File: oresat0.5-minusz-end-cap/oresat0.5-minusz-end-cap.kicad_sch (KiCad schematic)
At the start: 35 parts, among them J1 M55-7011242R, J2 U.FL-R-SMA, U1 LTC4305, U2 MMC5983MA, U3 MMC5983MA

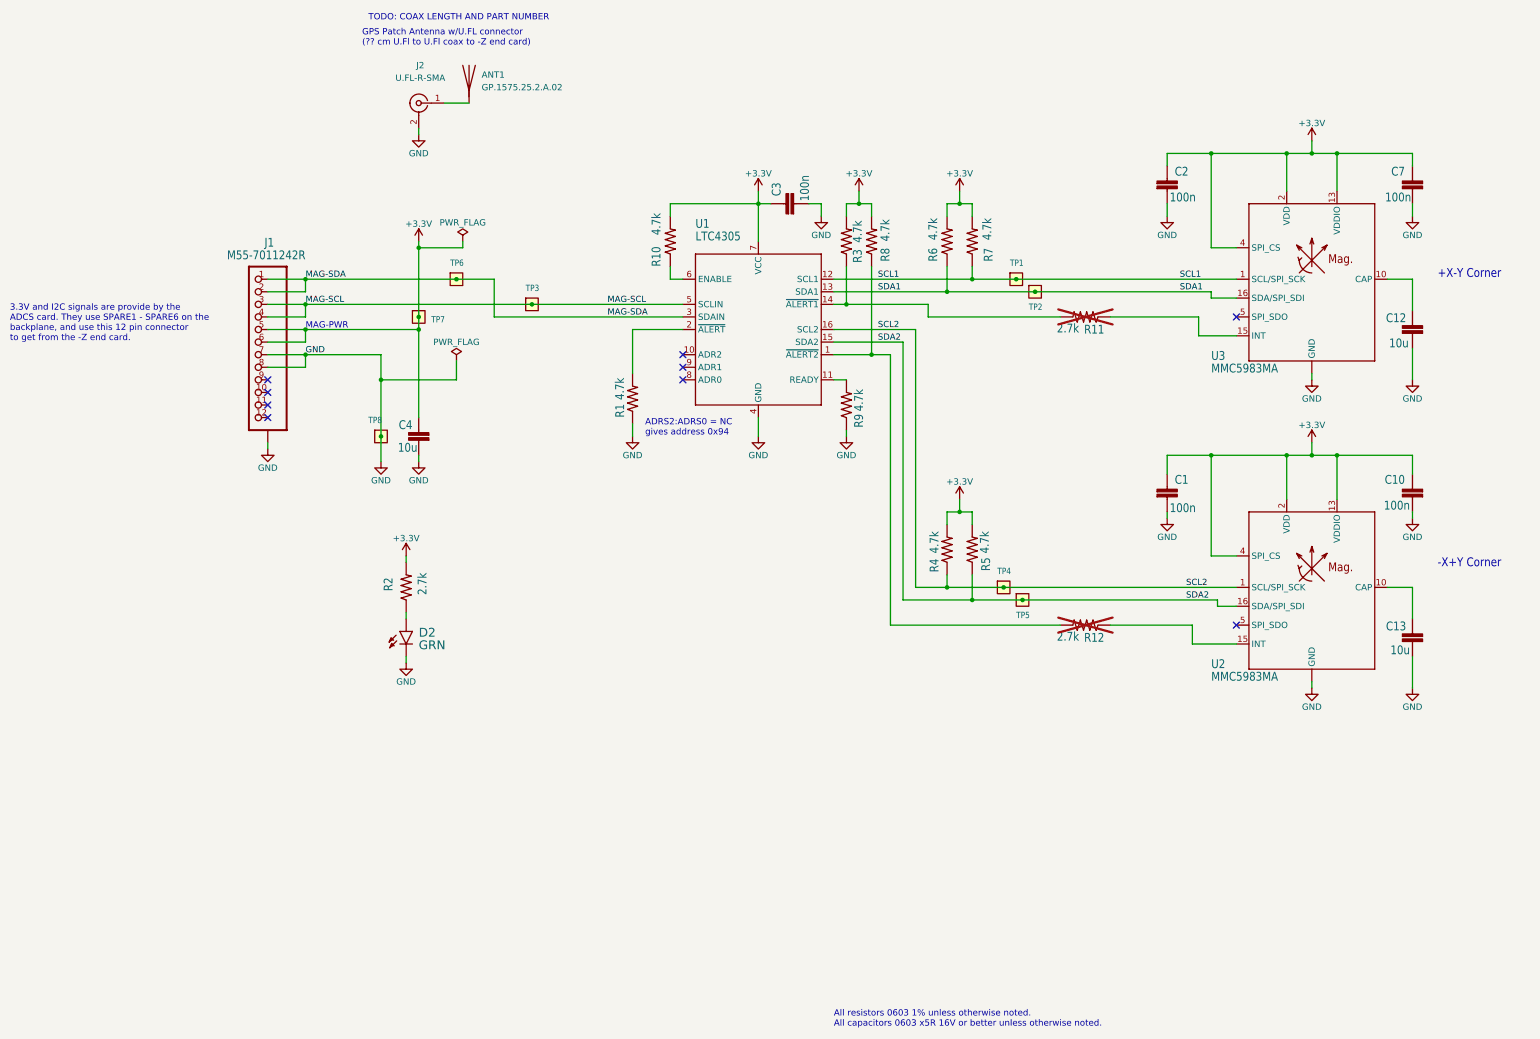
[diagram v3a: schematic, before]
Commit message: Added note on which MAG was which for firmware (PZ1 - MZ2).
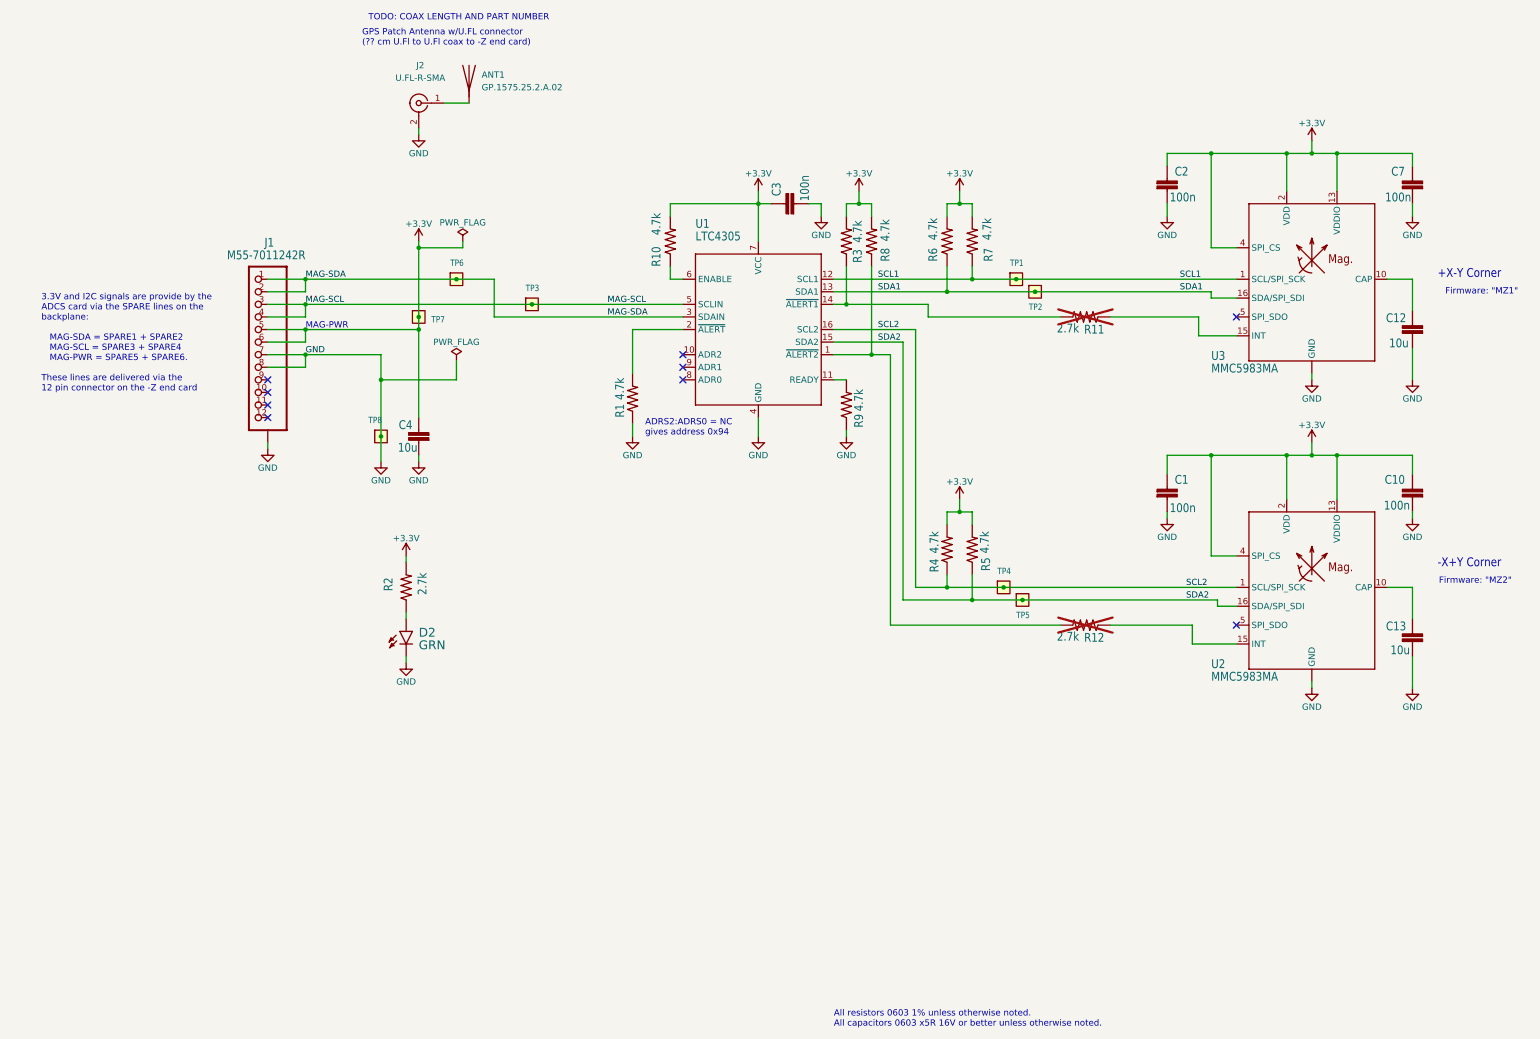
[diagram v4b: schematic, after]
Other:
- note added: "3.3V and I2C signals are provide by the ADCS card via the SPARE lines on the backplane: MAG-SDA = SPARE1 + SPARE2 MAG-SCL = SPARE3 + SPARE4 MAG-PWR = SPARE5 + SPARE6. These lines are delivered via the 12 pin connector on the -Z end card"
- note added: "Firmware: "MZ1""
- note added: "Firmware: "MZ2""
- note removed: "3.3V and I2C signals are provide by the ADCS card. They use SPARE1 - SPARE6 on the backplane, and use this 12 pin connector to get from the -Z end card."
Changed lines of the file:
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@@
 		)
 	)
-	(text "3.3V and I2C signals are provide by the \nADCS card. They use SPARE1 - SPARE6 on the\nbackplane, and use this 12 pin connector \nto get from the -Z end card."
+	(text "3.3V and I2C signals are provide by the \nADCS card via the SPARE lines on the \nbackplane:\n\n   MAG-SDA = SPARE1 + SPARE2\n   MAG-SCL = SPARE3 + SPARE4 \n   MAG-PWR = SPARE5 + SPARE6.\n\nThese lines are delivered via the \n12 pin connector on the -Z end card"
 		(exclude_from_sim no)
-		(at 41.91 124.46 0)
+		(at 48.26 134.62 0)
 		(effects
 			(font
@@
 			)
 			(justify left bottom)
+		)
+	)
+	(text "Firmware: \"MZ1\""
+		(exclude_from_sim no)
+		(at 339.09 114.3 0)
+		(effects
+			(font
+				(size 1.27 1.27)
+			)
 		)
 	)
@@
 		)
 	)
+	(text "Firmware: \"MZ2\""
+		(exclude_from_sim no)
+		(at 337.82 172.72 0)
+		(effects
+			(font
+				(size 1.27 1.27)
+			)
+		)
+	)

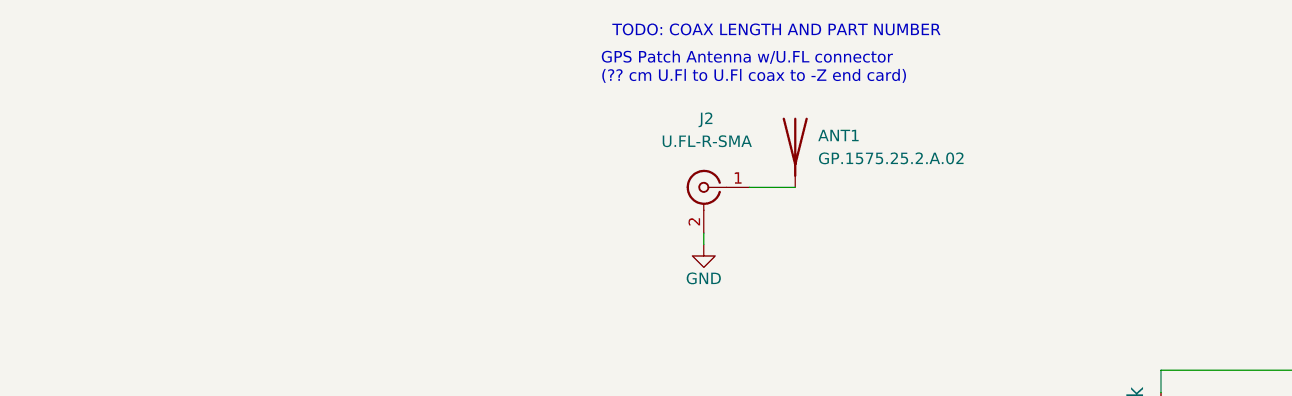
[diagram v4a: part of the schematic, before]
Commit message: More information on end cap RF, including coax jumper for end cap.
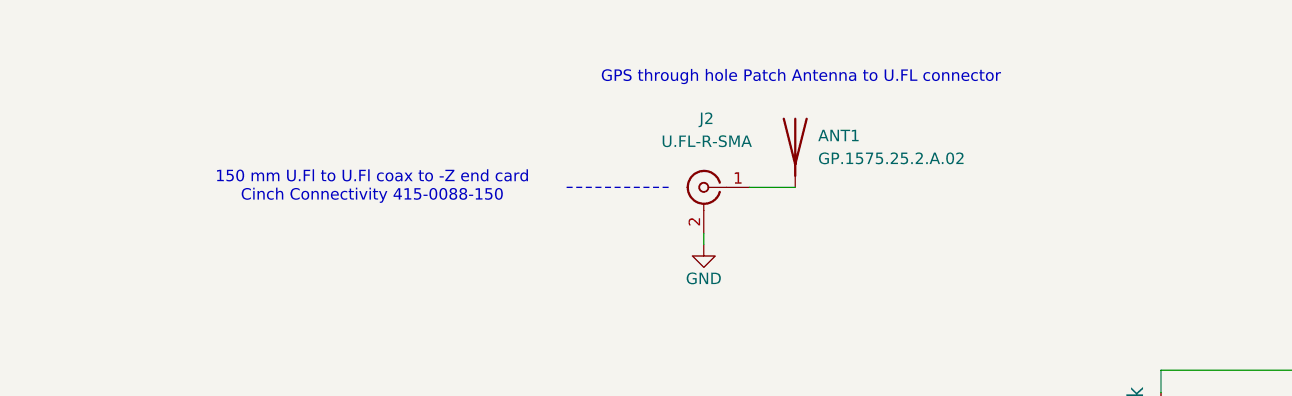
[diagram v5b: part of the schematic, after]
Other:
- note added: "150 mm U.Fl to U.Fl coax to -Z end card Cinch Connectivity 415-0088-150"
- note added: "GPS through hole Patch Antenna to U.FL connector"
- note removed: "GPS Patch Antenna w/U.FL connector (?? cm U.Fl to U.Fl coax to -Z end card)"
- note removed: "TODO: COAX LENGTH AND PART NUMBER"
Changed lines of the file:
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@@
+		)
+	)
+	(polyline
+		(pts
+			(xy 109.22 76.2) (xy 120.65 76.2)
+		)
+		(stroke
+			(width 0)
+			(type dash)
 		)
 	)
@@
 			(width 0)
 			(type default)
+		)
+	)
+	(text "150 mm U.Fl to U.Fl coax to -Z end card\nCinch Connectivity 415-0088-150\n"
+		(exclude_from_sim no)
+		(at 87.63 76.2 0)
+		(effects
+			(font
+				(size 1.27 1.27)
+			)
+			(href "https://www.cinch.com/media/drawings/products/rf-microwave/cable-assemblies/cable-assembly/dr-ccs-john-415-0088-150.pdf")
 		)
 	)
@@
 		)
 	)
-	(text "GPS Patch Antenna w/U.FL connector\n(?? cm U.Fl to U.Fl coax to -Z end card)\n"
+	(text "GPS through hole Patch Antenna to U.FL connector\n"
 		(exclude_from_sim no)
 		(at 113.03 64.77 0)
@@
 			)
 			(justify left bottom)
-		)
-	)
-	(text "TODO: COAX LENGTH AND PART NUMBER"
-		(exclude_from_sim no)
-		(at 114.3 59.69 0)
-		(effects
-			(font
-				(size 1.27 1.27)
-				(color 255 0 0 1)
-			)
-			(justify left bottom)

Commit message: Updated BOM to include MFR/MPN/etc.
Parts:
- ANT1: DPN (none) -> 931-1016-ND; DST (none) -> Digi-Key; MFR (none) -> Taoglas Limited; MPN (none) -> GP.1575.25.2.A.02
- C1, C10, C2, C3, C7: DPN (none) -> 587-3472-1-ND; DST (none) -> Digi-Key; MFR (none) -> Taiyo Yuden; MPN (none) -> TMK107BJ104KAHT
- C12, C13, C4: DPN (none) -> 490-12317-1-ND; DST (none) -> Digi-Key; MFR (none) -> Murata; MPN (none) -> GRT188R61C106KE13D
- D2: DPN (none) -> 732-4971-1-ND; DST (none) -> Digi-Key; MFR (none) -> Wurth; MPN (none) -> 150060GS75000
- J1: DPN (none) -> 952-3875-1-ND; DST (none) -> Digi-Key; MFR (none) -> Harwin; MPN (none) -> M55-7011242R
- J2: DPN (none) -> H11891CT-ND; DST (none) -> Digi-Key; MFR (none) -> Hirose; MPN (none) -> U.FL-R-SMT-1(10)
- R1, R10, R3, R4, R5, R6, R7, R8, R9: DPN (none) -> RMCF0603FT4K70CT-ND; DST (none) -> Digi-Key; MFR (none) -> Stackpole Electronics Inc; MPN (none) -> RMCF0603FT4K70
- R11, R12, R2: DPN (none) -> RMCF0603FT2K70CT-ND; DST (none) -> Digi-Key; MFR (none) -> Stackpole Electronics Inc; MPN (none) -> RMCF0603FT2K70
- TP1, TP2, TP3, TP4, TP5, TP6, TP7, TP8: value TEST-POINT-LARGE-SQUARE -> Test-Point; DPN (none) -> N/A; DST (none) -> N/A; MFR (none) -> N/A; MPN (none) -> N/A; now left out of the parts list
- U1: DPN (none) -> LTC4305IGN#PBF-ND; DST (none) -> Digi-Key; MFR (none) -> Analog Devices; MPN (none) -> LTC4305IGN#PBF
- U2, U3: DPN (none) -> 1267-1072-1-ND; DST (none) -> Digi-Key; MFR (none) -> Memsic; MPN (none) -> MMC5883MA
